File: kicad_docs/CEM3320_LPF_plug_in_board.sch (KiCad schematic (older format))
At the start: 42 parts, among them J1 signal_in, J2 signal_in, J3 signal_out, J4 Conn_01x08_Male, U1 CEM3320, U2 TL072

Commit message: fix silkscreen issue where R8 and R6 refs overlapped
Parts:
- U1: symbol my_parts:CEM3320 -> CEM3320_LPF_plug_in_board-rescue:CEM3320-my_parts
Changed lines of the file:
@@
 $EndDescr
 $Comp
-L my_parts:CEM3320 U1
+L CEM3320_LPF_plug_in_board-rescue:CEM3320-my_parts U1
 U 1 1 5CFC321B
 P 3150 1900
@@
 $EndComp
 $Comp
-L my_parts:CEM3320 U1
+L CEM3320_LPF_plug_in_board-rescue:CEM3320-my_parts U1
 U 5 1 5CFCA84C
 P 5400 4850
@@
 $EndComp
 $Comp
-L my_parts:CEM3320 U1
+L CEM3320_LPF_plug_in_board-rescue:CEM3320-my_parts U1
 U 6 1 5CFCB180
 P 7150 4200
@@
 $EndComp
 $Comp
-L my_parts:CEM3320 U1
+L CEM3320_LPF_plug_in_board-rescue:CEM3320-my_parts U1
 U 7 1 5CFCBB67
 P 3750 6900
@@
 	2500 1350 3000 1350
 $Comp
-L my_parts:CEM3320 U1
+L CEM3320_LPF_plug_in_board-rescue:CEM3320-my_parts U1
 U 2 1 5CFE101D
 P 4950 1900
@@
 	4300 2400 4300 2300
 $Comp
-L my_parts:CEM3320 U1
+L CEM3320_LPF_plug_in_board-rescue:CEM3320-my_parts U1
 U 3 1 5CFE7D31
 P 6750 1900
@@
 	6100 2400 6100 2300
 $Comp
-L my_parts:CEM3320 U1
+L CEM3320_LPF_plug_in_board-rescue:CEM3320-my_parts U1
 U 4 1 5CFF2FBA
 P 8550 1900

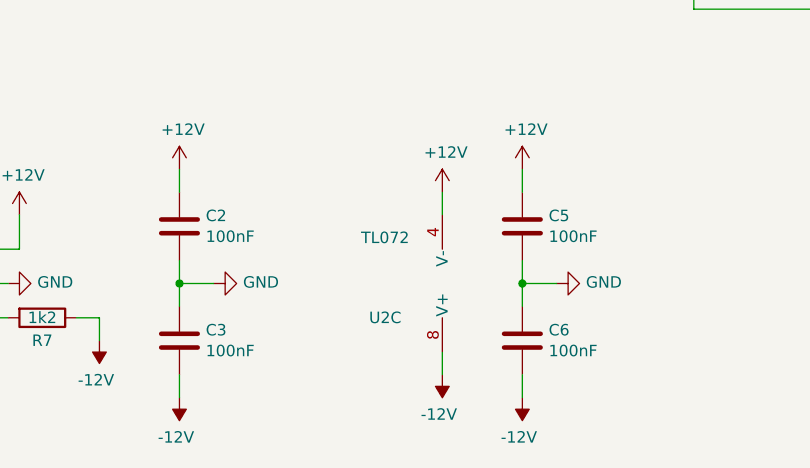
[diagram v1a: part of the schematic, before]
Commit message: fix reversed power pins on TL072 in schm and brd, delete bad gerbers
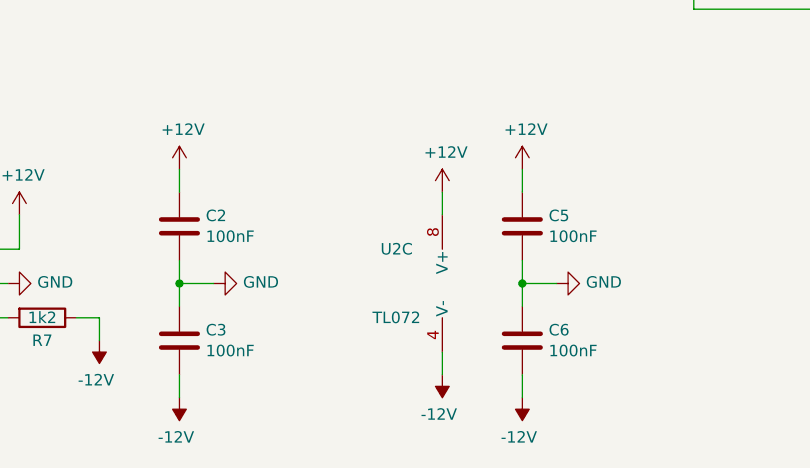
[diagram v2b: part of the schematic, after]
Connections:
- net +12V: now also U2.8 (V+); no longer U2.4 (V-)
- net -12V: now also U2.4 (V-); no longer U2.8 (V+)
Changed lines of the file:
@@
 L Amplifier_Operational:TL072 U2
 U 3 1 5D6AB760
-P 5850 6900
-F 0 "U2" H 6000 7050 50  0000 C CNN
-F 1 "TL072" H 6000 6700 50  0000 C CNN
-F 2 "Package_SO:SOIC-8_3.9x4.9mm_P1.27mm" H 5850 6900 50  0001 C CNN
-F 3 "http://www.ti.com/lit/ds/symlink/tl071.pdf" H 5850 6900 50  0001 C CNN
-	3    5850 6900
-	-1   0    0    1
+P 6050 6900
+F 0 "U2" H 5750 7050 50  0000 C CNN
+F 1 "TL072" H 5750 6750 50  0000 C CNN
+F 2 "Package_SO:SOIC-8_3.9x4.9mm_P1.27mm" H 6050 6900 50  0001 C CNN
+F 3 "http://www.ti.com/lit/ds/symlink/tl071.pdf" H 6050 6900 50  0001 C CNN
+	3    6050 6900
+	1    0    0    -1
 $EndComp
 $Comp
